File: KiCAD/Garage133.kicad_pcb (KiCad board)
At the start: 4 copper layers, 82.5 x 39.4 mm, 44 parts, among them J1 Edge2x6_Connector, J2 USB_B_Micro, K1 SANYOU_SRD_Form_C, K2 SANYOU_SRD_Form_C, Q2 UMH3N, Q3 MMBT3906, Q4 MMBT3906, U1 ESP32-WROOM-32, U2 AMS1117-3.3, U3 SHTC3

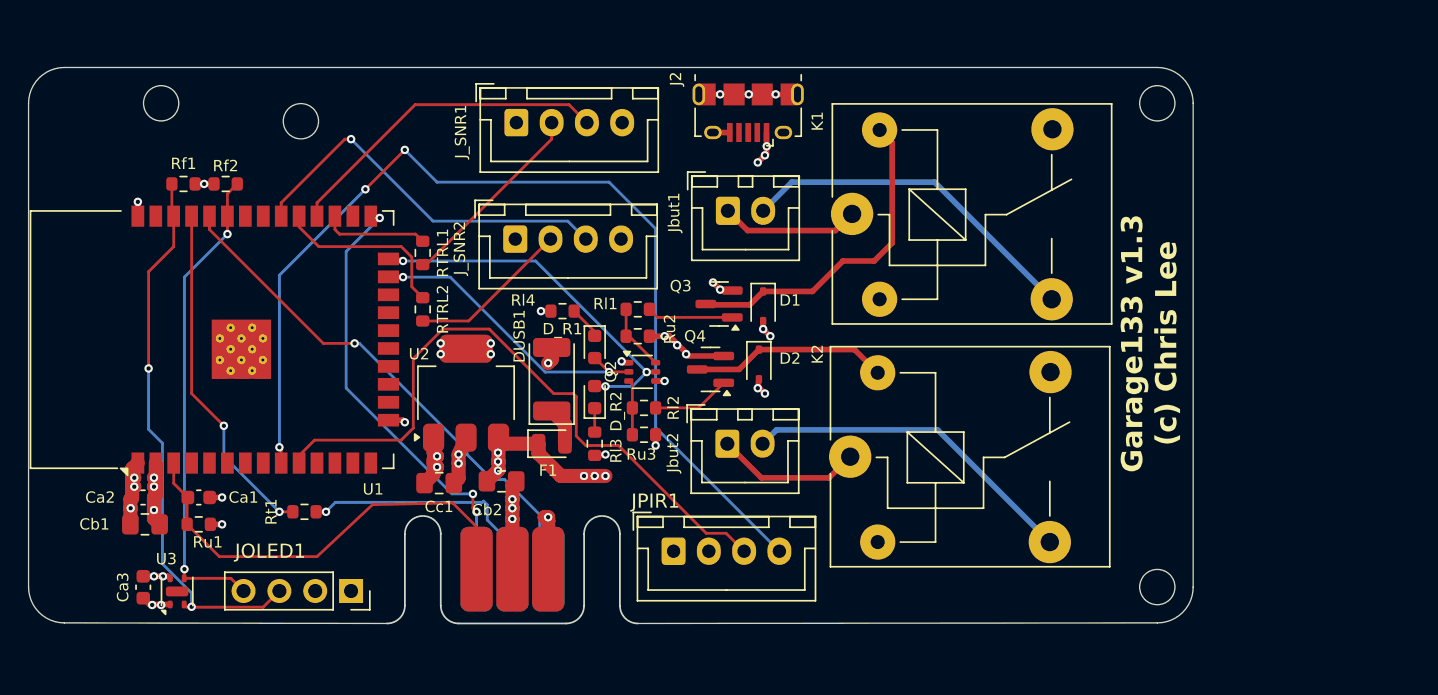
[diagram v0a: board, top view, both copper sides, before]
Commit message: four-sonar board (#25)
The four-sonar board written about in [Dual Sonar ESP32 Garage State
Estimation](https://selectiveappeal.org/posts/garage133-dual-sonar/).

- Board supports front and back sonars for both right and left garage
bays.
- Software update for dual-observation hmm, training update.
  - Distinct states for door open with car present and not present.
- Updated ebox design, sencil fixture
- Updated device web interface
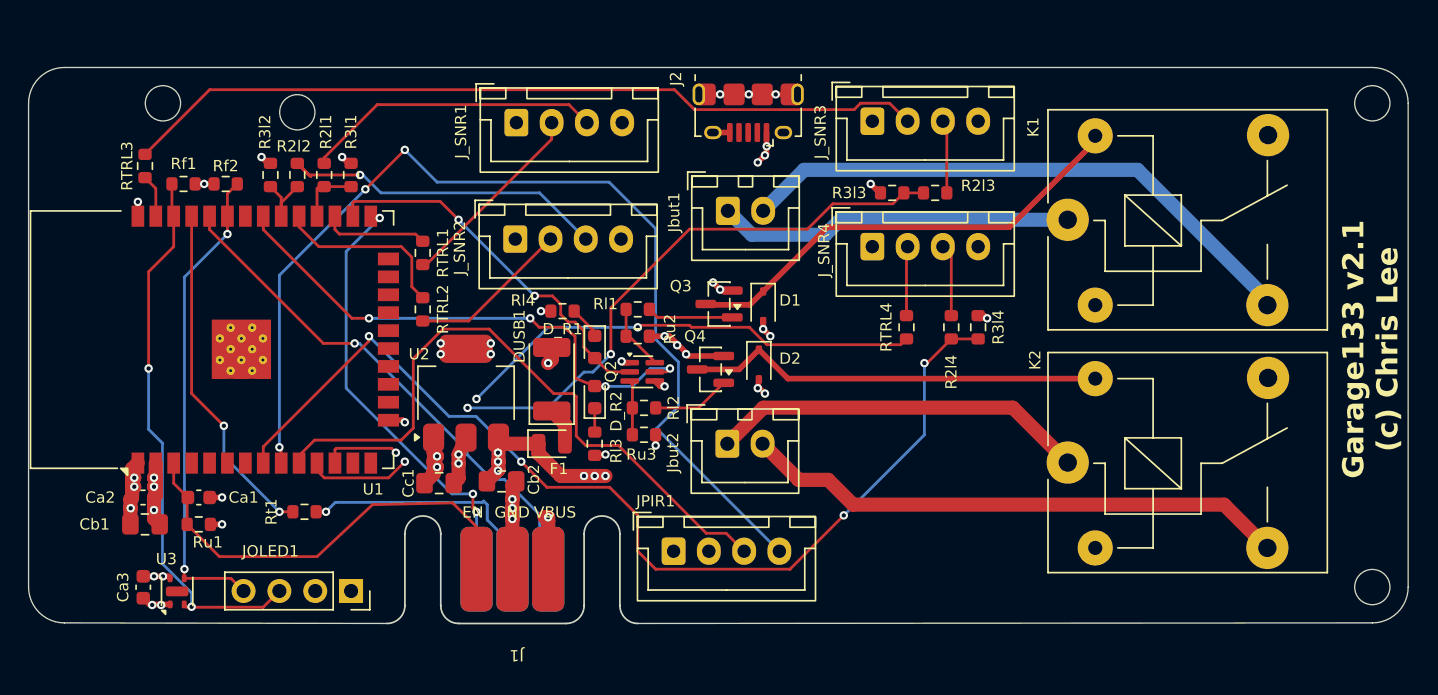
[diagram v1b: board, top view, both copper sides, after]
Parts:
- removed the REF** at (70.4, 50.8)
- removed the REF** at (141.0, 50.8)
- removed the REF** at (141.0, 85.1)
- removed the REF** at (80.3, 52.1)
- added J_SNR3: Conn_01x04_Pin, Connector_JST:JST_XH_B4B-XH-A_1x04_P2.50mm_Vertical, F.Cu at (120.8, 52.1)
- added J_SNR4: Conn_01x04_Pin, Connector_JST:JST_XH_B4B-XH-A_1x04_P2.50mm_Vertical, F.Cu at (120.8, 61.0)
- added R2l1: 2.2k, Resistor_SMD:R_0603_1608Metric, F.Cu at (81.9, 55.9)
- added R2l2: 2.2k, Resistor_SMD:R_0603_1608Metric, F.Cu at (80.0, 55.9)
- added R2l3: 2.2k, Resistor_SMD:R_0603_1608Metric, F.Cu at (125.2, 57.1)
- added R2l4: 2.2k, Resistor_SMD:R_0603_1608Metric, F.Cu at (126.4, 66.7)
- added R3l1: 3.3k, Resistor_SMD:R_0603_1608Metric, F.Cu at (83.8, 55.9)
- added R3l2: 3.3k, Resistor_SMD:R_0603_1608Metric, F.Cu at (78.1, 55.9)
- added R3l3: 3.3k, Resistor_SMD:R_0603_1608Metric, F.Cu at (122.2, 57.1)
- added R3l4: 3.3k, Resistor_SMD:R_0603_1608Metric, F.Cu at (128.3, 66.7)
- added REF**: MountingHole_2.5mm, MountingHole:MountingHole_2.5mm, F.Cu at (156.2, 85.1)
- added REF**: MountingHole_2.5mm, MountingHole:MountingHole_2.5mm, F.Cu at (80.0, 51.4)
- added REF**: MountingHole_2.5mm, MountingHole:MountingHole_2.5mm, F.Cu at (156.2, 50.8)
- added REF**: MountingHole_2.5mm, MountingHole:MountingHole_2.5mm, F.Cu at (70.5, 50.8)
- added RTRL3: 1k, Resistor_SMD:R_0603_1608Metric, F.Cu at (69.2, 55.2)
- added RTRL4: 1k, Resistor_SMD:R_0603_1608Metric, F.Cu at (123.2, 66.7)
- J1: footprint Library:EdgeConnector_2x3 -> chl33_library:EdgeConnector_2x3
- moved K2 15.4 mm to (134.6, 76.3)
- moved K1 15.3 mm to (134.6, 59.1)
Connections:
- J_SNR1 pad 3: ECHO1 -> Net-(J_SNR1-Pin_3)
- J_SNR2 pad 3: ECHO2 -> Net-(J_SNR2-Pin_3)
- U1 pad 11: unconnected-(U1-IO26-Pad11) -> ECHO3
- U1 pad 12: unconnected-(U1-IO27-Pad12) -> TRIG4
- U1 pad 23: RELAY_CMD1 -> unconnected-(U1-IO15-Pad23)
- U1 pad 24: RELAY_CMD2 -> unconnected-(U1-IO2-Pad24)
- U1 pad 26: unconnected-(U1-IO4-Pad26) -> RELAY_CMD1
- U1 pad 31: unconnected-(U1-IO19-Pad31) -> RELAY_CMD2
- U1 pad 37: unconnected-(U1-IO23-Pad37) -> TRIG3
- U1 pad 8: unconnected-(U1-IO32-Pad8) -> ECHO4
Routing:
- net ECHO4: track 0.00 -> 73.3 mm, vias 0 -> 4
- net Net-(J_SNR3-Pin_2): track 0.00 -> 57.3 mm
- net ECHO3: track 0.00 -> 54.0 mm, vias 0 -> 3
- net TRIG4: track 0.00 -> 46.1 mm, vias 0 -> 3
- net Net-(J_SNR2-Pin_3): track 0.00 -> 24.0 mm, vias 0 -> 1
- net ECHO2: track 27.3 -> 4.98 mm, vias 1 -> 0
- net Net-(J_SNR1-Pin_3): track 0.00 -> 21.1 mm
- net ECHO1: track 23.5 -> 4.32 mm
- net RELAY2A: track 10.3 -> 27.1 mm
- net RELAY1B: track 24.7 -> 41.1 mm
- net Net-(D2-K): track 14.0 -> 29.6 mm
- net RELAY1A: track 9.87 -> 25.3 mm
- net RELAY2B: track 24.1 -> 39.1 mm
- net RELAY_CMD2: track 26.4 -> 37.7 mm, vias 3 -> 4
- net Net-(D1-K): track 23.8 -> 33.1 mm
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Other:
- board size 82.5 x 39.4 mm -> 97.8 x 39.4 mm
- board text added: "+5"
- board text added: "AL"
- board text added: "ECH"
- board text added: "EN"
- board text added: "GND"
- board text added: "GPIO"
- board text added: "Garage133 v2.1 (c) Chris Lee"
- board text added: "M1"
- board text added: "RX"
- board text added: "SCL"
- board text added: "SDA"
- board text added: "TRIG"
- board text added: "TX"
- board text added: "VBUS"
- board text removed: "Garage133 v1.3 (c) Chris Lee"

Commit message: KiCAD board v3.0 changes (I think)
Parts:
- removed J2: USB_B_Micro, Connector_USB:USB_Micro-B_Amphenol_10118194_Horizontal
- removed the REF** at (80.0, 51.4)
- removed the REF** at (156.2, 50.8)
- removed Rt1: 470, Resistor_SMD:R_0603_1608Metric
- added R_cc1: 5.1k, Resistor_SMD:R_0603_1608Metric, F.Cu at (82.9, 55.5)
- added R_cc2: 5.1k, Resistor_SMD:R_0603_1608Metric, F.Cu at (89.2, 58.9)
- DUSB1: footprint Diode_SMD:D_2010_5025Metric -> Diode_SMD:D_SMA
- J1: value Edge2x6_Connector -> USB_C_Receptacle_USB2.0_16P; footprint chl33_library:EdgeConnector_2x3 -> Connector_USB:USB_C_Receptacle_HRO_TYPE-C-31-M-12
- U1: value ESP32-WROOM-32 -> ESP32-S3-WROOM-1; footprint RF_Module:ESP32-WROOM-32 -> RF_Module:ESP32-S3-WROOM-1
- moved RTRL3 44.5 mm to (113.7, 56.6), turned to 0 degrees
- moved J1 34.2 mm to (91.3, 52.4)
- moved Rf1 25.9 mm to (81.9, 80.4), turned to 180 degrees
- moved Jbut1 25.8 mm to (104.9, 83.6)
- moved Rf2 23.2 mm to (81.9, 78.6)
- moved JPIR1 16.9 mm to (89.8, 83.6)
- moved Jbut2 9.71 mm to (114.9, 83.6)
- moved J_SNR4 5.46 mm to (115.3, 60.7)
- moved J_SNR2 5.38 mm to (100.8, 60.7)
- moved J_SNR1 5.35 mm to (100.8, 51.4)
- moved J_SNR3 5.10 mm to (115.7, 51.6)
- moved REF** 4.70 mm to (151.5, 85.0)
- moved K1 4.49 mm to (130.1, 59.1)
- moved K2 4.49 mm to (130.1, 76.3)
- moved D1 4.14 mm to (113.6, 69.3)
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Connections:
- Cb1 pad 1: +3.3V -> +5V
- Cb2 pad 1: +5V -> +3.3V
- U1 pad 11: ECHO3 -> unconnected-(U1-IO18-Pad11)
- U1 pad 12: TRIG4 -> SDA1
- U1 pad 13: unconnected-(U1-IO14-Pad13) -> USB_D-
- U1 pad 14: unconnected-(U1-IO12-Pad14) -> USB_D+
- U1 pad 15: GND -> TRIG3
- U1 pad 17: unconnected-(U1-SHD/SD2-Pad17) -> SCL1
- U1 pad 18: unconnected-(U1-SWP/SD3-Pad18) -> RELAY_CMD1
- U1 pad 19: unconnected-(U1-SCS/CMD-Pad19) -> RELAY_CMD2
- U1 pad 20: unconnected-(U1-SCK/CLK-Pad20) -> AL
- U1 pad 25: GPIO0 -> unconnected-(U1-IO48-Pad25)
- U1 pad 26: RELAY_CMD1 -> unconnected-(U1-IO45-Pad26)
- U1 pad 27: TRIG1 -> unconnected-(U1-IO0-Pad27)
- U1 pad 28: ECHO1 -> unconnected-(U1-IO35-Pad28)
- U1 pad 29: TRIG2 -> unconnected-(U1-IO36-Pad29)
- U1 pad 30: ECHO2 -> unconnected-(U1-IO37-Pad30)
- U1 pad 31: RELAY_CMD2 -> unconnected-(U1-IO38-Pad31)
- U1 pad 33: SDA1 -> unconnected-(U1-IO40-Pad33)
- U1 pad 34: TXC -> unconnected-(U1-IO41-Pad34)
- U1 pad 35: TX -> unconnected-(U1-IO42-Pad35)
- U1 pad 36: SCL1 -> unconnected-(U1-RXD0-Pad36)
- U1 pad 37: TRIG3 -> unconnected-(U1-TXD0-Pad37)
- U1 pad 38: GND -> TRIG2
- U1 pad 39: GND -> TRIG1
- U1 pad 4: unconnected-(U1-SENSOR_VP-Pad4) -> TRIG4
- U1 pad 5: unconnected-(U1-SENSOR_VN-Pad5) -> ECHO1
- U1 pad 6: unconnected-(U1-IO34-Pad6) -> ECHO2
- U1 pad 7: unconnected-(U1-IO35-Pad7) -> ECHO3
- U1 pad 9: AL -> unconnected-(U1-IO16-Pad9)
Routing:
- net Net-(J_SNR3-Pin_2): track 57.3 -> 6.62 mm
- net AL: track 73.8 -> 27.9 mm, vias 3 -> 2
- net TRIG3: track 3.05 -> 46.8 mm, vias 0 -> 2
- net TXC: track 37.0 -> 0.00 mm, vias 1 -> 0
- net ECHO1: track 4.32 -> 36.0 mm, vias 0 -> 2
- net GPIO0: track 31.3 -> 0.00 mm, vias 3 -> 0
- net M1: track 46.8 -> 19.7 mm, vias 0 -> 2
- net EN: track 31.4 -> 4.78 mm
- net USB_D+: track 0.00 -> 26.4 mm, vias 0 -> 2
- net USB_D-: track 0.00 -> 26.3 mm
- net ECHO2: track 4.98 -> 29.9 mm, vias 0 -> 2
- net TX: track 24.3 -> 0.00 mm, vias 2 -> 0
- net VBUS: track 41.2 -> 20.3 mm, vias 5 -> 2
- net RELAY1A: track 25.3 -> 44.5 mm
- net +5V: track 38.6 -> 57.6 mm, vias 12 -> 14
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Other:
- board size 97.8 x 39.4 mm -> 93.3 x 39.4 mm
- board text added: "Garage133 v3.0 (c) Chris Lee"
- board text removed: "EN"
- board text removed: "GPIO"
- board text removed: "Garage133 v2.1 (c) Chris Lee"
- board text removed: "RX"
- board text removed: "TX"
- board text removed: "VBUS"

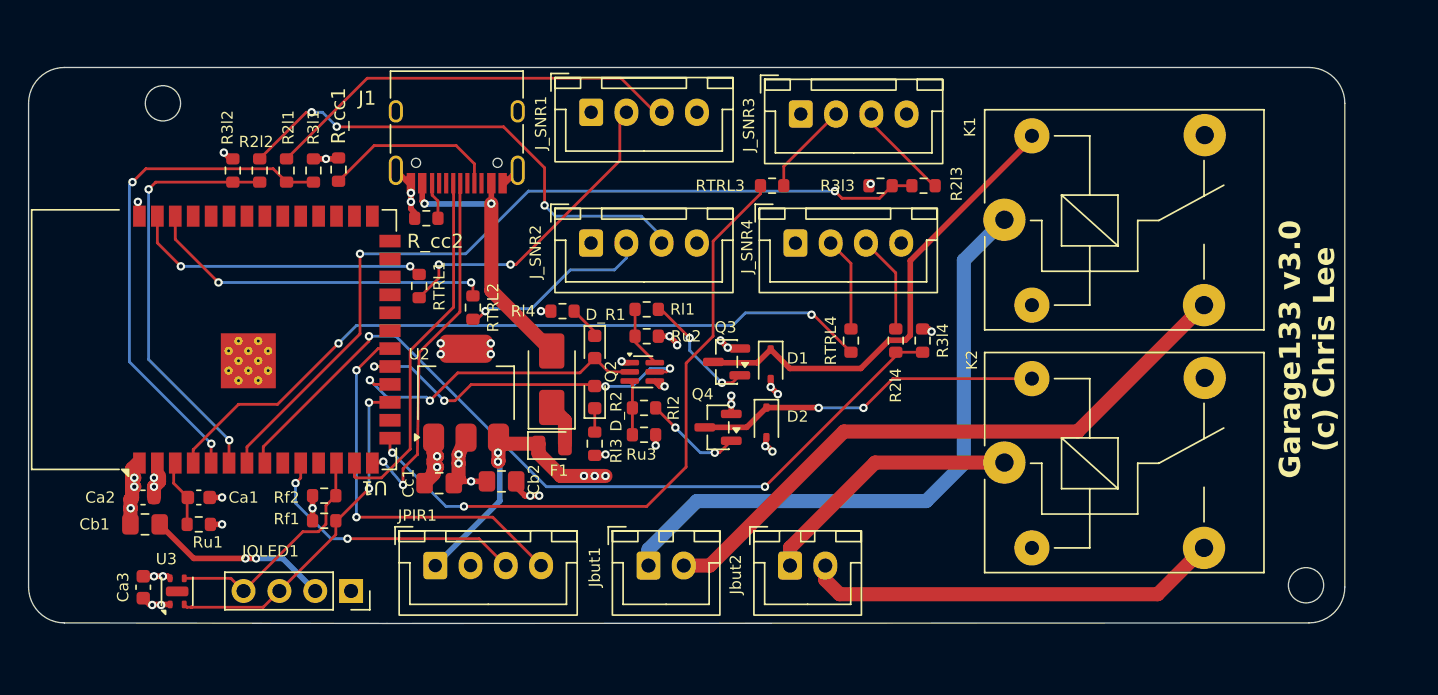
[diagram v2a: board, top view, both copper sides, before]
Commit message: PCB updates: board v3.1
- USB-C connect other side D+,D-
- Move USB-C to stick-out from board
- Push buttons for EN and PROG
- Move connectors away from OLED
- Move SHTC3 away from ESP32, to far side of relays. Thermal isolation milling.
- M2.5 hole for OLED support.
- Replace MMBT3906 transistors with MMBT4403 on Gemini recommendation.
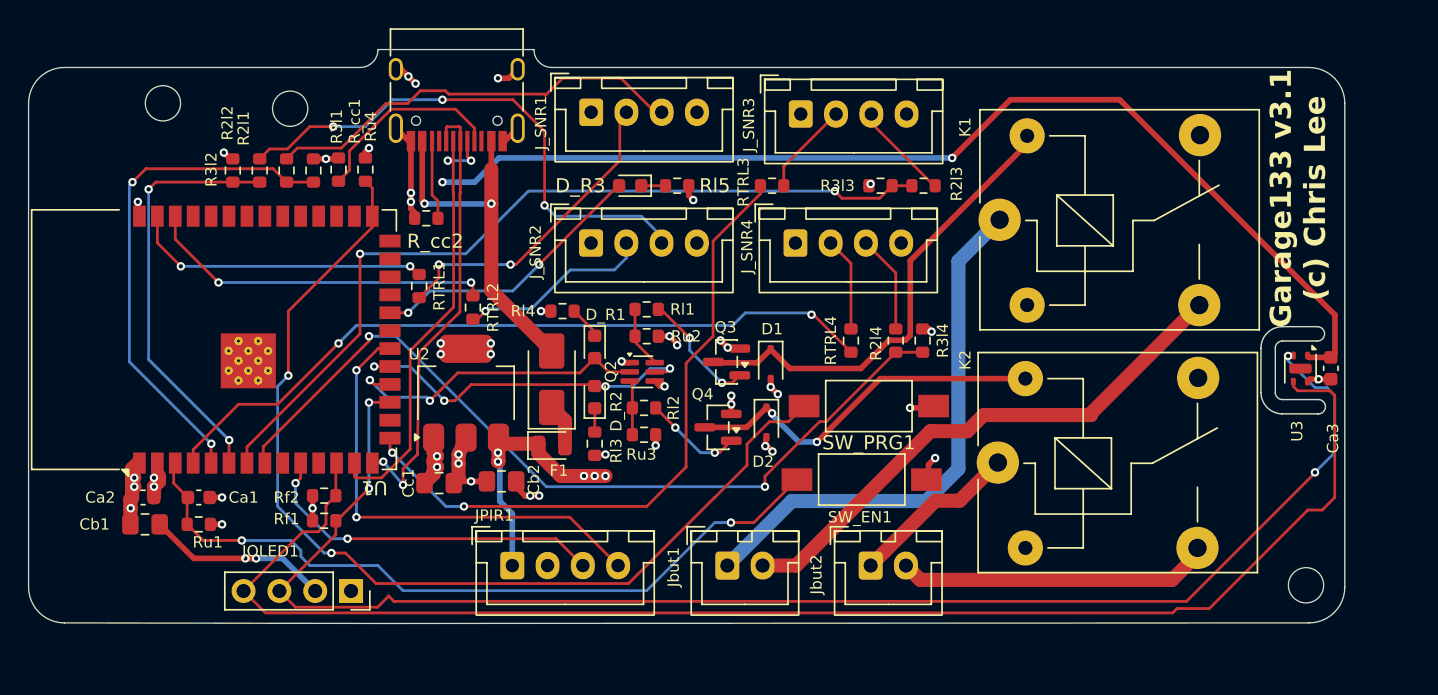
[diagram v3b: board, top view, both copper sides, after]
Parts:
- added D_R3: YLW, LED_SMD:LED_0603_1608Metric, F.Cu at (103.6, 56.6)
- added REF**: MountingHole_2.5mm, MountingHole:MountingHole_2.5mm, F.Cu at (79.5, 51.2)
- added Rl5: 1k, Resistor_SMD:R_0603_1608Metric, F.Cu at (106.9, 56.6)
- added Ru4: 10k, Resistor_SMD:R_0603_1608Metric, F.Cu at (84.8, 55.5)
- added SW_EN1: SW_Push, Button_Switch_SMD:SW_SPST_FSMSM, F.Cu at (120.0, 77.5)
- added SW_PRG1: SW_Push, Button_Switch_SMD:SW_SPST_FSMSM, F.Cu at (120.5, 72.3)
- D1, D2: value D -> B5817WS-TP
- Q3, Q4: value MMBT3906 -> MMBT4403
- moved Ca3 85.6 mm to (153.3, 69.6), turned to -90 degrees
- moved U3 81.2 mm to (151.1, 69.6), turned to -90 degrees
- moved Jbut2 5.72 mm to (120.7, 83.6)
- moved Jbut1 5.59 mm to (110.5, 83.6)
- moved JPIR1 5.46 mm to (95.2, 83.6)
- moved J1 2.98 mm to (91.3, 49.4)
- moved K2 0.46 mm to (129.7, 76.3)
- moved K1 0.34 mm to (129.8, 59.1)
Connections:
- net EN renamed Net-(U1-EN)
- J1 pad B6: unconnected-(J1-D+-PadB6) -> USB_D+
- J1 pad B7: unconnected-(J1-D--PadB7) -> USB_D-
- U1 pad 22: unconnected-(U1-IO14-Pad22) -> LED1
- U1 pad 27: unconnected-(U1-IO0-Pad27) -> Net-(U1-IO0)
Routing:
- net SDA1: track 17.0 -> 104.6 mm
- net SCL1: track 24.9 -> 106.7 mm, vias 2 -> 4
- net +3.3V: track 12.3 -> 87.8 mm, vias 13 -> 14
- net Net-(U1-IO0): track 0.00 -> 71.7 mm, vias 0 -> 2
- net Net-(U1-EN): track 4.78 -> 53.5 mm, vias 0 -> 2
- net GND: track 29.6 -> 50.1 mm, vias 25 -> 30
- net LED1: track 0.00 -> 20.0 mm, vias 0 -> 2
- net RELAY2B: track 29.6 -> 22.3 mm
- net RELAY2A: track 19.0 -> 12.5 mm
- net USB_D-: track 26.3 -> 32.4 mm, vias 0 -> 2
- net RELAY1A: track 44.5 -> 38.4 mm
- net USB_D+: track 26.4 -> 32.0 mm
- net VBUS: track 20.3 -> 25.9 mm
- net RELAY1B: track 44.5 -> 39.0 mm
- net AL: track 27.9 -> 33.4 mm
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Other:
- board size 93.3 x 39.4 mm -> 93.3 x 40.7 mm
- board text added: "Garage133 v3.1 (c) Chris Lee"
- board text removed: "Garage133 v3.0 (c) Chris Lee"
